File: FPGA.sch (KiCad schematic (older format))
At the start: 16 parts, among them U14 SiT8008B, U8 GW1N-9LQ100

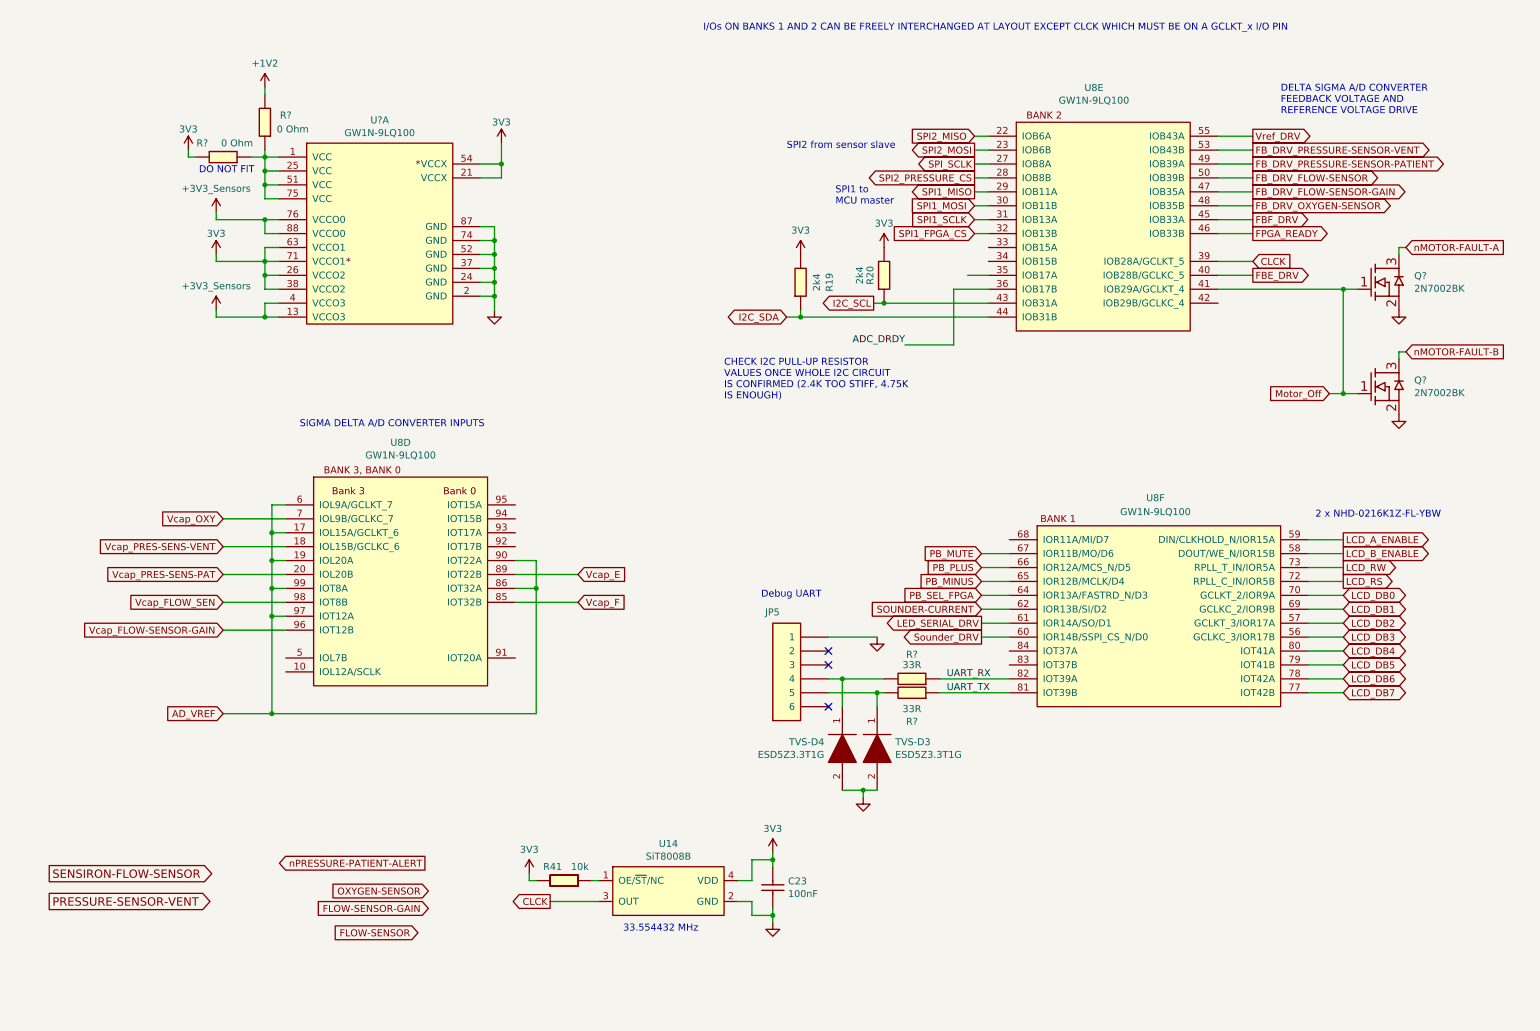
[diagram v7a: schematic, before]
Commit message: Moved FPGA decoupling caps to FPGA sheet. Deleted FPGA JTAG SPECIAL PWR sheet as now empty
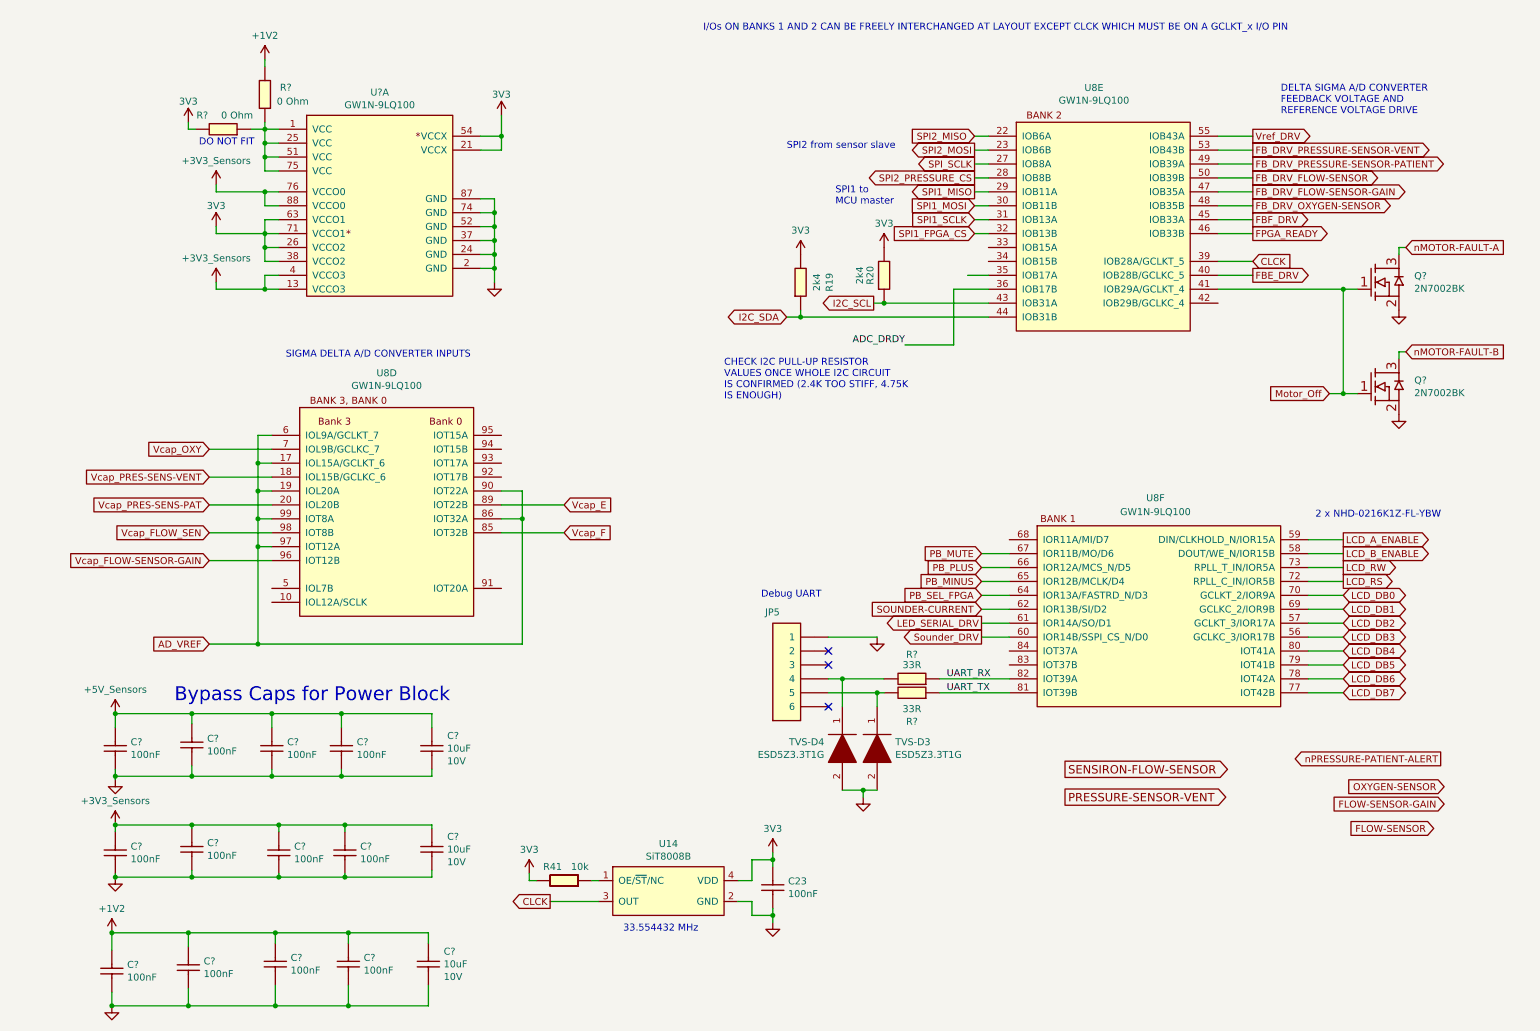
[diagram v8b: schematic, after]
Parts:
- added C? (x3): 10uF_0805_Ceramic_Capacitor_10%_X7R_10V, Capacitor_SMD:C_0805_2012Metric, symbol OpenVent:10uF_0805_Ceramic_Capacitor_10%_X7R_10V
- added C? (x12): 100nF_0603_Ceramic_Capacitor,_10%,_X7R,_25V, symbol OpenVent:100nF_0603_Ceramic_Capacitor,_10%,_X7R,_25V
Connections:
- net +3.3V: now also C?.1, C?.1, C?.1, C?.1, C?.1
- net +5V: now also C?.1, C?.1, C?.1, C?.1, C?.1, C?.1, C?.1, C?.1, C?.1, C?.1
- net GND: now also C?.2, C?.2, C?.2, C?.2, C?.2, C?.2, C?.2, C?.2, C?.2, C?.2, C?.2, C?.2, C?.2, C?.2, C?.2
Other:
- note added: "Bypass Caps for Power Block"
- moved on the sheet: R?, U8D, U?A
